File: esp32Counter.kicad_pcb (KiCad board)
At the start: 2 copper layers, 19 parts, among them J1 Jack-DC, J2 USB<->ttl, J3 SPI_CONN, J4 GPIO_2_4_5, SW1 SW_Push, SW2 SW_Push, U1 AMS1117-3.3, U2 ESP-07

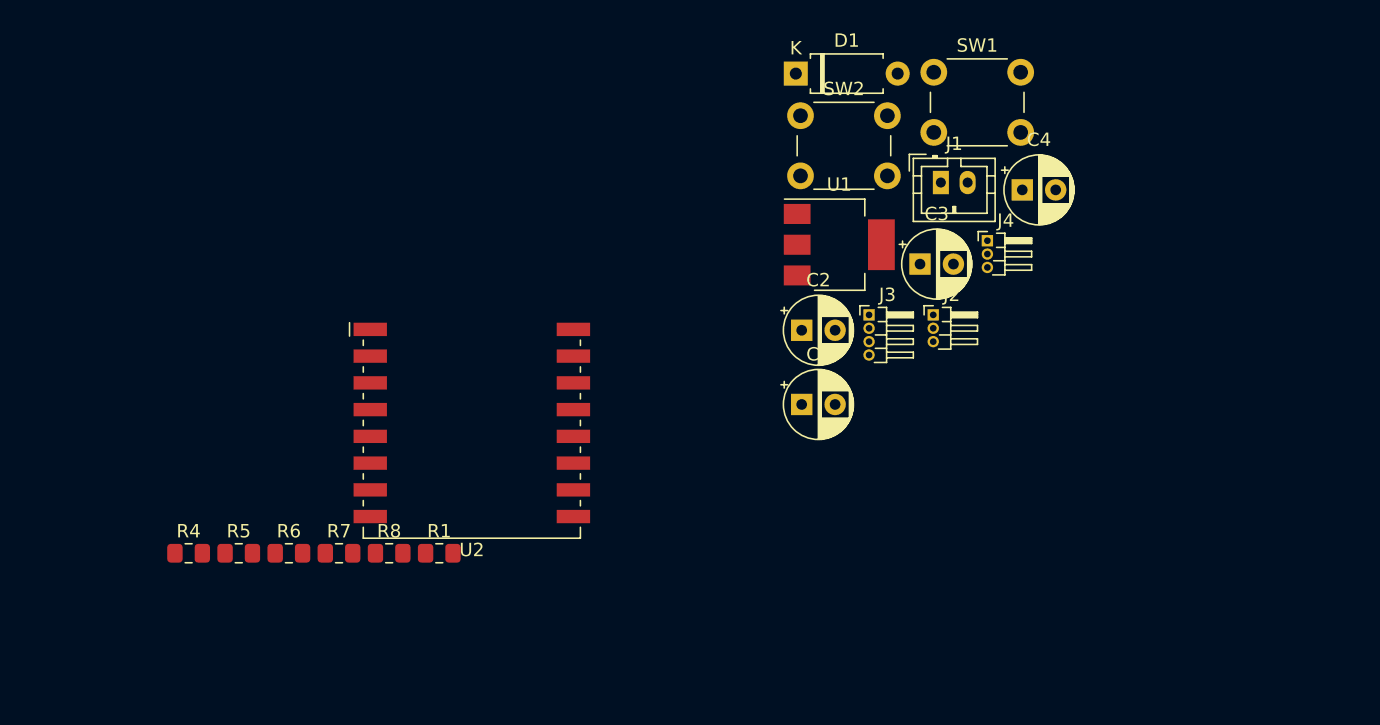
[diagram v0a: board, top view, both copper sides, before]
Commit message: v1.0 with tatal camoacitor
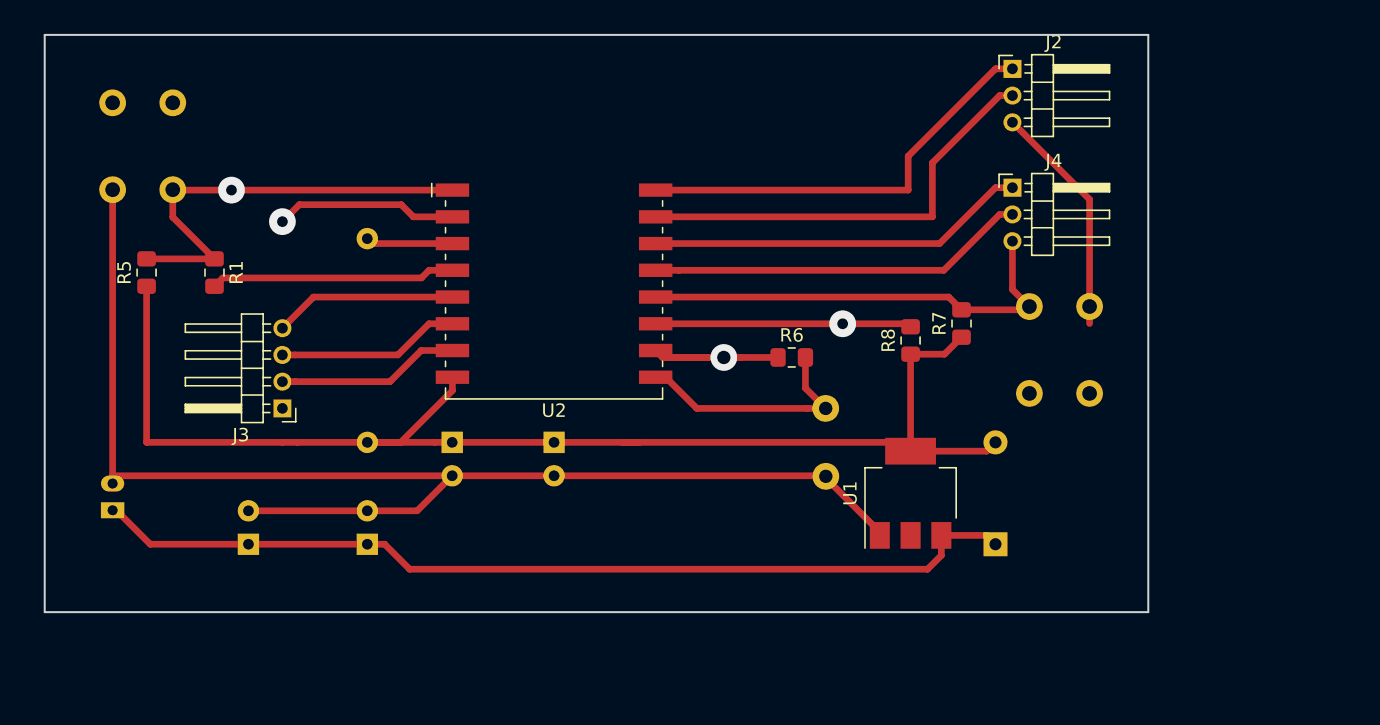
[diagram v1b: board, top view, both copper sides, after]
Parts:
- added F1: Fuse, Fuse:Fuseholder_TR5_Littlefuse_No560_No460, B.Cu at (72.4, 40.6)
- C1, C3, C4, D1, J1, SW1, SW2: moved to B.Cu
- C2: value 100uF -> 10uF; moved to B.Cu
- J2: footprint Connector_PinHeader_1.00mm:PinHeader_1x03_P1.00mm_Horizontal -> Connector_PinHeader_2.00mm:PinHeader_1x03_P2.00mm_Horizontal
- J3: footprint Connector_PinHeader_1.00mm:PinHeader_1x04_P1.00mm_Horizontal -> Connector_PinHeader_2.00mm:PinHeader_1x04_P2.00mm_Horizontal
- J4: value GPIO_2_4_5 -> GPIO_5_4_0; footprint Connector_PinHeader_1.00mm:PinHeader_1x03_P1.00mm_Horizontal -> Connector_PinHeader_2.00mm:PinHeader_1x03_P2.00mm_Horizontal
- R4: footprint Resistor_SMD:R_0805_2012Metric_Pad1.15x1.40mm_HandSolder -> Resistor_THT:R_Axial_DIN0207_L6.3mm_D2.5mm_P15.24mm_Horizontal; moved to B.Cu
- moved J1 66.6 mm to (19.1, 48.3), turned to 90 degrees
- moved SW1 61.5 mm to (19.1, 17.8), turned to 270 degrees
- moved C3 54.4 mm to (29.2, 50.8), turned to 90 degrees
- moved R7 49.6 mm to (82.5, 34.3), turned to 90 degrees
- moved J3 44.4 mm to (31.8, 40.6), turned to 180 degrees
- moved R8 42.1 mm to (78.7, 35.6), turned to 90 degrees
- moved R6 40.4 mm to (69.8, 36.8)
- moved C4 39.8 mm to (52.1, 43.2), turned to 270 degrees
- moved D1 38.2 mm to (85.1, 50.8), turned to 90 degrees
- moved C1 34.1 mm to (38.1, 50.8), turned to 90 degrees
- moved C2 27.5 mm to (44.5, 43.2), turned to 270 degrees
- moved R1 26.9 mm to (26.7, 30.5), turned to 270 degrees
- moved SW2 22.3 mm to (87.6, 33.0), turned to 270 degrees
- moved R5 22.1 mm to (21.6, 30.5), turned to 90 degrees
- moved U1 19.3 mm to (78.7, 47.0), turned to 90 degrees
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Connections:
- J3 pad 1: /HSPI_MISO -> Net-(J3-Pad1)
- J3 pad 3: /HSPI_CLK -> /HSPI_MISO
- J3 pad 4: /HSPICS -> /HSPI_CLK
- J4 pad 1: /GPIO2 -> /GPIO5
- J4 pad 3: /GPIO5 -> /GIPO0
- R6 pad 2: Net-(C1-Pad2) -> Net-(F1-Pad1)
- R7 pad 2: Net-(R7-Pad2) -> /GIPO0
- SW2 pad 1: Net-(R7-Pad2) -> /GIPO0
- U2 pad 12: Net-(R7-Pad2) -> /GIPO0
- U2 pad 9: Net-(C1-Pad2) -> Net-(F1-Pad1)
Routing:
- net Net-(C1-Pad2): track 0.00 -> 97.2 mm
- net Net-(C2-Pad1): track 0.00 -> 96.6 mm
- net Net-(C1-Pad1): track 0.00 -> 70.1 mm
- net /GIPO0: track 0.00 -> 33.9 mm
- net /RXtoTX: track 0.00 -> 32.8 mm
- net Net-(R1-Pad1): track 0.00 -> 32.7 mm, vias 0 -> 1
- net /TXtoRX: track 0.00 -> 31.9 mm
- net /GPIO4: track 0.00 -> 28.4 mm
- net /GPIO5: track 0.00 -> 28.4 mm
- net /GPIO2: track 0.00 -> 19.2 mm, vias 0 -> 1
- net Net-(F1-Pad1): track 0.00 -> 18.5 mm
- net /deepsleep: track 0.00 -> 18.3 mm
- net Net-(J2-Pad3): track 0.00 -> 17.4 mm
- net /HSPICS: track 0.00 -> 15.2 mm, vias 0 -> 1
- net /HSPI_MOSI: track 0.00 -> 13.7 mm
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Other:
- board outline added: 82.5 x 43.2 mm

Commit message: v1.01
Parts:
- J2, J4: footprint Connector_PinHeader_2.00mm:PinHeader_1x03_P2.00mm_Horizontal -> Connector_PinHeader_2.54mm:PinHeader_1x03_P2.54mm_Horizontal; moved to B.Cu
- J3: footprint Connector_PinHeader_2.00mm:PinHeader_1x04_P2.00mm_Horizontal -> Connector_PinHeader_2.54mm:PinHeader_1x04_P2.54mm_Horizontal; moved to B.Cu
- moved SW2 11.7 mm to (90.2, 44.5)
- moved J4 8.89 mm to (86.4, 33.0)
- moved J2 7.62 mm to (86.4, 22.9)
- moved J3 6.48 mm to (33.0, 34.3)
- moved R6 1.80 mm to (71.1, 38.1)
- moved C4 1.80 mm to (53.3, 44.5)
- moved R8 1.80 mm to (80.0, 36.8)
- moved U1 1.80 mm to (80.0, 48.3)
- moved C3 1.80 mm to (30.5, 52.1)
- moved J1 1.80 mm to (20.3, 49.5)
- moved U2 1.80 mm to (53.3, 30.5)
- moved C1 1.80 mm to (39.4, 52.1)
- moved C2 1.80 mm to (45.7, 44.5)
- moved D1 1.80 mm to (86.4, 52.1)
- moved R1 1.80 mm to (27.9, 31.8)
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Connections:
- J2 pad 1: /TXtoRX -> Net-(J2-Pad1)
- J2 pad 3: Net-(J2-Pad3) -> /TXtoRX
- J3 pad 1: Net-(J3-Pad1) -> /HSPI_CLK
- J3 pad 2: /HSPI_MOSI -> /HSPI_MISO
- J3 pad 3: /HSPI_MISO -> /HSPI_MOSI
- J3 pad 4: /HSPI_CLK -> Net-(J3-Pad4)
- J4 pad 1: /GPIO5 -> /GIPO0
- J4 pad 3: /GIPO0 -> /GPIO5
- SW2 pad 2: Net-(J2-Pad3) -> Net-(J2-Pad1)
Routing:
- net Net-(J2-Pad1): track 0.00 -> 25.8 mm
- net Net-(J2-Pad3): track 17.4 -> 0.00 mm
- net /GIPO0: track 33.9 -> 39.5 mm
- net /RXtoTX: track 32.8 -> 30.1 mm
- net /GPIO4: track 28.4 -> 25.9 mm
- net /GPIO5: track 28.4 -> 26.1 mm
- net /TXtoRX: track 31.9 -> 30.1 mm
- net /HSPI_CLK: track 13.7 -> 13.0 mm
- net (no net): vias 0 -> 4
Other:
- board size 82.5 x 43.2 mm -> 99.1 x 49.5 mm
- board text added: "ESP-07"
